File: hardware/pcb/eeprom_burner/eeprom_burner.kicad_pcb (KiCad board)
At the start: 2 copper layers, 68.6 x 53.3 mm, 15 parts, among them P1 Power, P2 Analog, P3 Digital, P4 Digital, P5 CONN_01X01, P6 CONN_01X01, P7 CONN_01X01, P8 CONN_01X01, U1 74HC595, U2 74HC595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

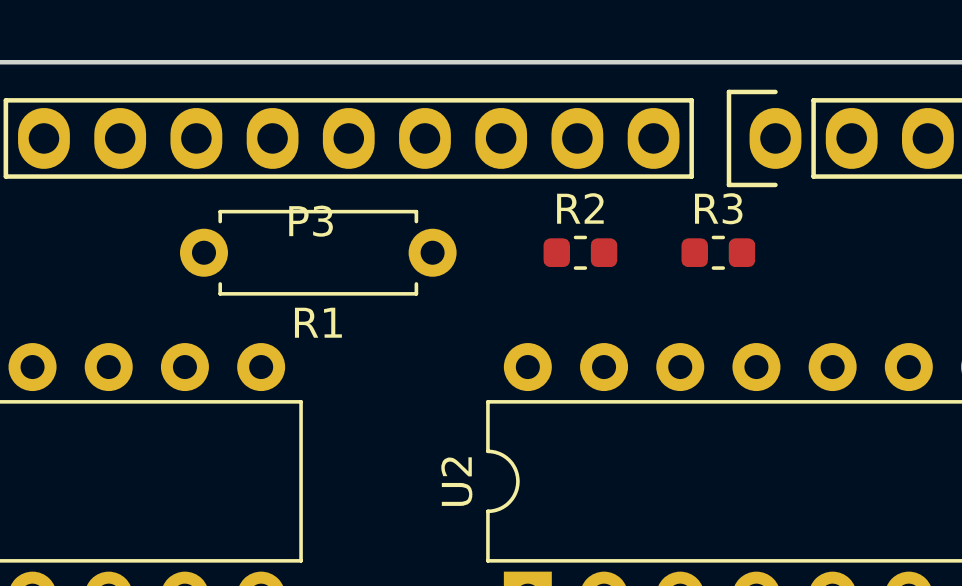
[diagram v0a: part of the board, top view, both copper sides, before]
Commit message: Update footprints, add solder jumper
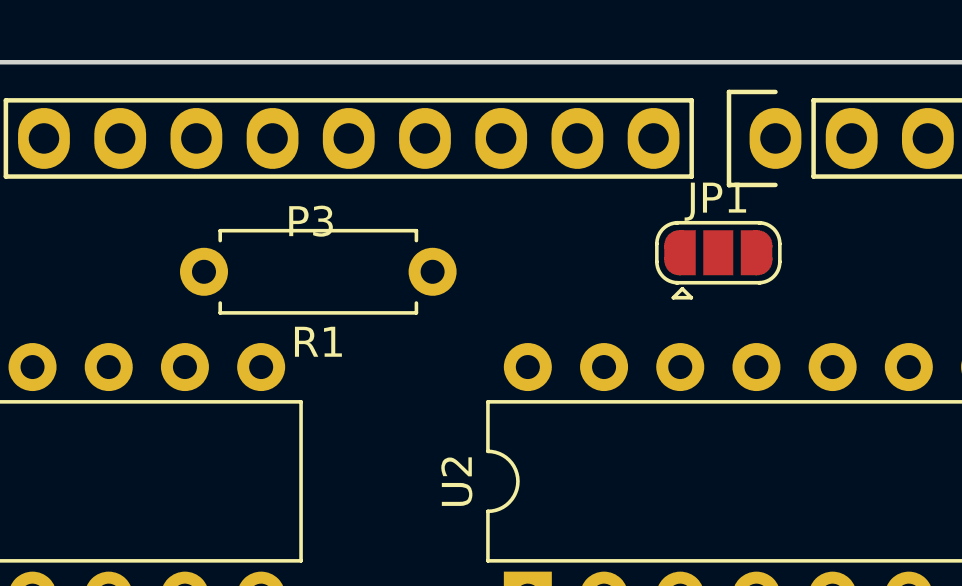
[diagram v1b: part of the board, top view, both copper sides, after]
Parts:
- removed R2, R3: R, Resistor_SMD:R_0603_1608Metric
- added JP1: SolderJumper_3_Open, Jumper:SolderJumper-3_P1.3mm_Open_RoundedPad1.0x1.5mm, F.Cu at (154.8, 79.4)
- R1: value R -> 10K
- moved R1 0.64 mm to (145.3, 80.0)

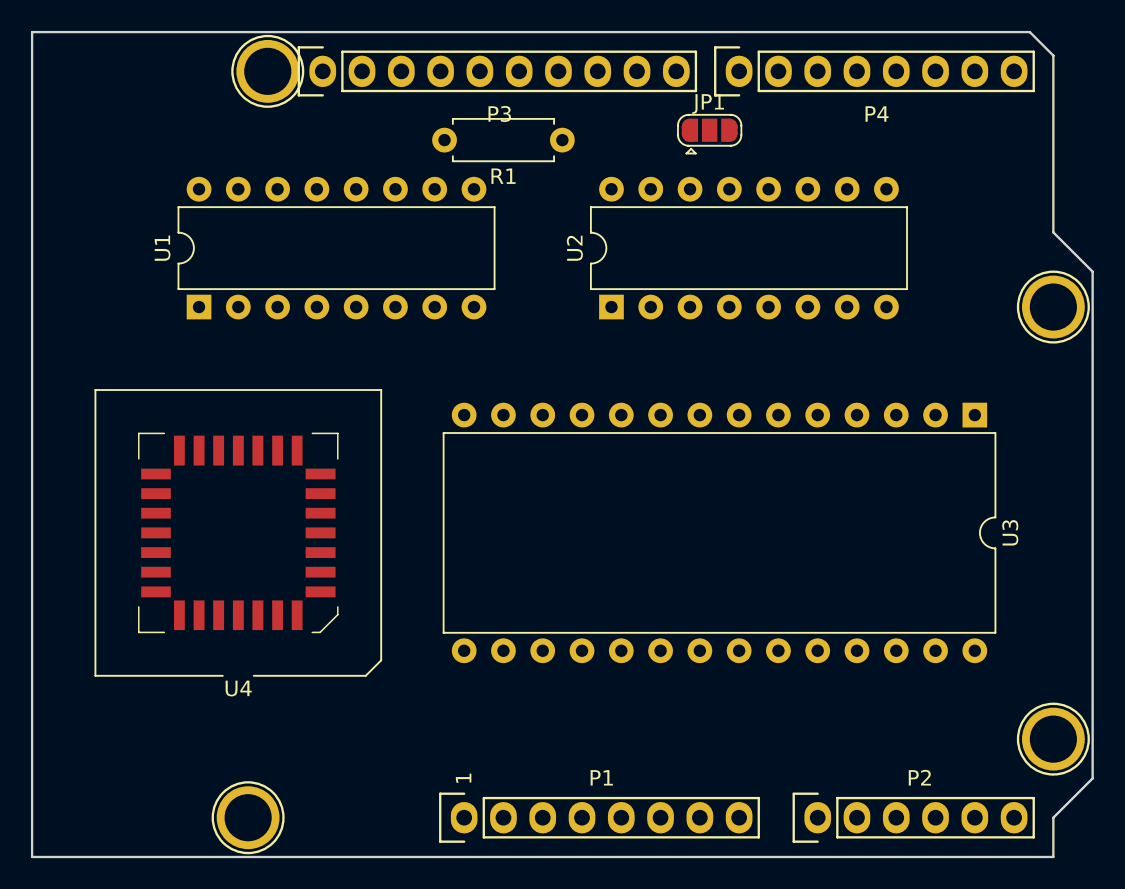
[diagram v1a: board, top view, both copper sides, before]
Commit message: Updated footprints - use generic headers
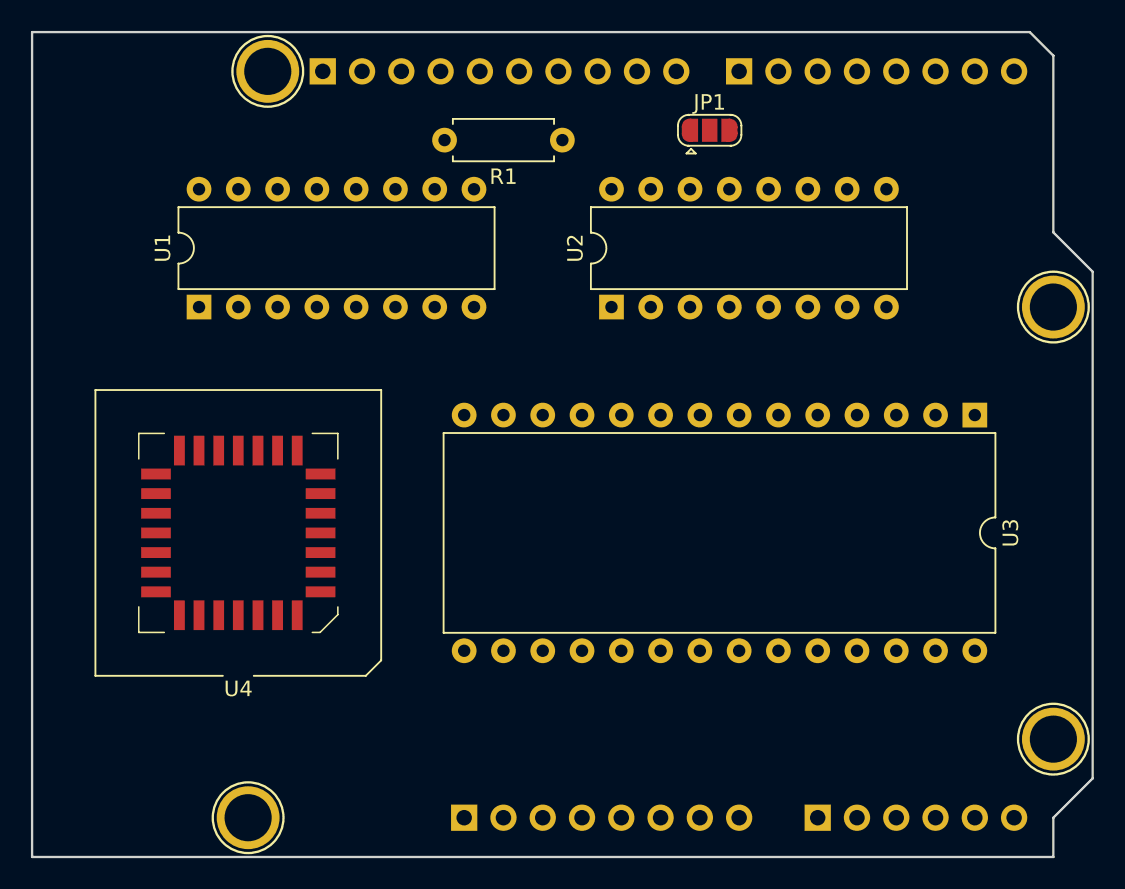
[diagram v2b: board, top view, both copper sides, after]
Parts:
- P1, P4: footprint Socket_Arduino_Uno:Socket_Strip_Arduino_1x08 -> Connector_PinHeader_2.54mm:PinHeader_1x08_P2.54mm_Vertical; moved to B.Cu
- P2: footprint Socket_Arduino_Uno:Socket_Strip_Arduino_1x06 -> Connector_PinHeader_2.54mm:PinHeader_1x06_P2.54mm_Vertical; moved to B.Cu
- P3: footprint Socket_Arduino_Uno:Socket_Strip_Arduino_1x10 -> Connector_PinHeader_2.54mm:PinHeader_1x10_P2.54mm_Vertical; moved to B.Cu
- turned P1 to 270 degrees
- turned P2 to 270 degrees
- turned P3 to 270 degrees
- turned P4 to 270 degrees
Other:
- board text removed: "1"

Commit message: Add output connectors
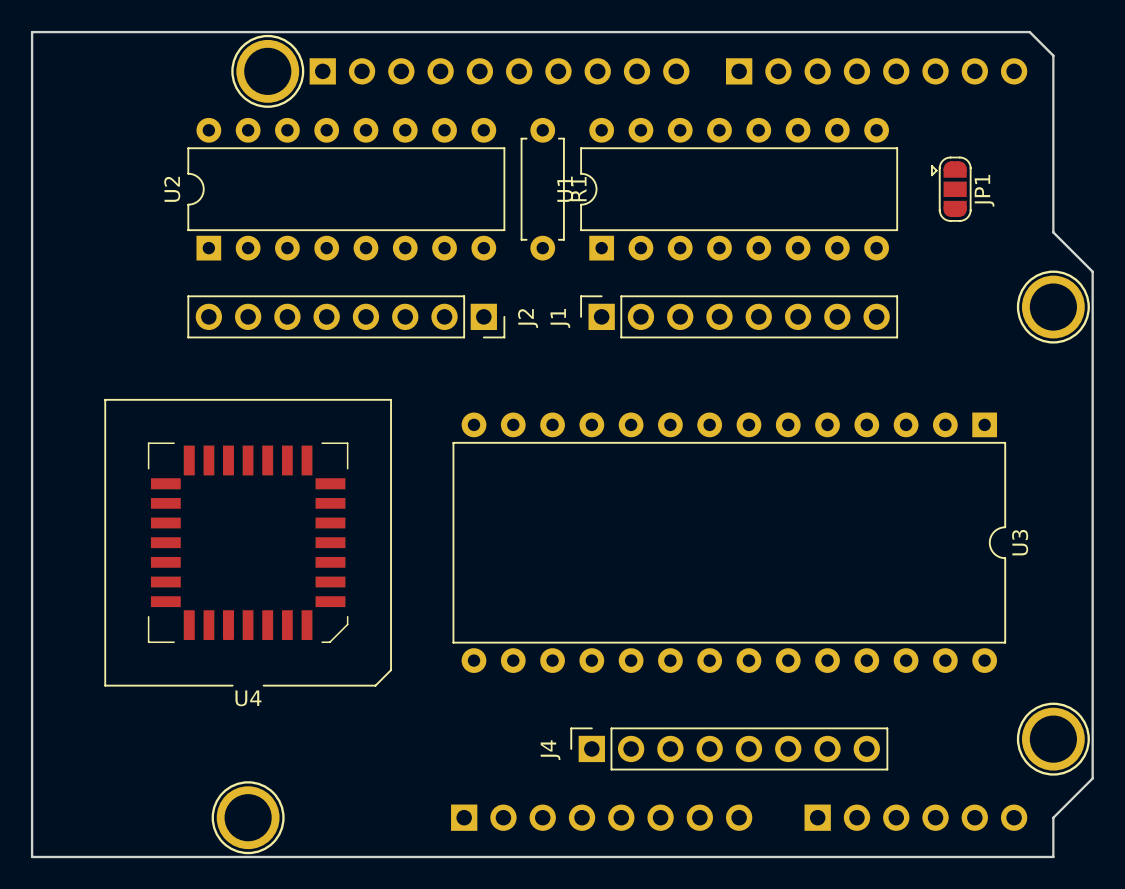
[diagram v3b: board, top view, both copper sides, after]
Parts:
- added J1: Conn_01x08, Connector_PinSocket_2.54mm:PinSocket_1x08_P2.54mm_Vertical, F.Cu at (147.8, 91.4)
- added J2: Conn_01x08, Connector_PinSocket_2.54mm:PinSocket_1x08_P2.54mm_Vertical, F.Cu at (140.2, 91.4)
- added J4: Conn_01x06, Connector_PinSocket_2.54mm:PinSocket_1x08_P2.54mm_Vertical, F.Cu at (147.2, 119.4)
- moved U1 26.3 mm to (147.8, 87.0)
- moved U2 26.3 mm to (122.4, 87.0)
- moved JP1 16.3 mm to (170.7, 83.2), turned to 270 degrees
- moved R1 1.42 mm to (144.0, 79.4), turned to 270 degrees
- moved U4 0.90 mm to (125.0, 106.0)
- moved U3 0.90 mm to (172.6, 98.4)
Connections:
- P2 pad 1: A0 -> E0
- P2 pad 2: A1 -> E1
- P2 pad 3: A2 -> E2
- P2 pad 4: A3 -> E3
- P2 pad 5: /A4(SDA) -> E4
- P2 pad 6: /A5(SCL) -> E5

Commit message: Replace LCC EEPROM with correct part
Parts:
- U4: value 28C256 -> 28C256J; footprint Package_LCC:PLCC-28_SMD-Socket -> Package_LCC:PLCC-32_11.4x14.0mm_P1.27mm
- moved U4 0.63 mm to (125.6, 106.0)
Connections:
- U4 pad 1: A14 -> Net-(U4-Pad1)
- U4 pad 10: A0 -> A1
- U4 pad 11: D0 -> A0
- U4 pad 12: D1 -> Net-(U4-Pad12)
- U4 pad 13: D2 -> D0
- U4 pad 14: GND -> D1
- U4 pad 15: D3 -> D2
- U4 pad 16: D4 -> GND
- U4 pad 17: D5 -> Net-(U4-Pad17)
- U4 pad 18: D6 -> D3
- U4 pad 19: D7 -> D4
- U4 pad 2: A12 -> A14
- U4 pad 20: GND -> D5
- U4 pad 21: A10 -> D6
- U4 pad 22: A15 -> D7
- U4 pad 23: A11 -> GND
- U4 pad 24: A9 -> A10
- U4 pad 25: A8 -> A15
- U4 pad 26: A13 -> Net-(U4-Pad26)
- U4 pad 27: ~WE~ -> A11
- U4 pad 28: +5V -> A9
- U4 pad 3: A7 -> A12
- U4 pad 4: A6 -> A7
- U4 pad 5: A5 -> A6
- U4 pad 6: A4 -> A5
- U4 pad 7: A3 -> A4
- U4 pad 8: A2 -> A3
- U4 pad 9: A1 -> A2
